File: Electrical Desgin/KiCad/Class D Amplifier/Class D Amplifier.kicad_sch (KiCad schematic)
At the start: 1 part

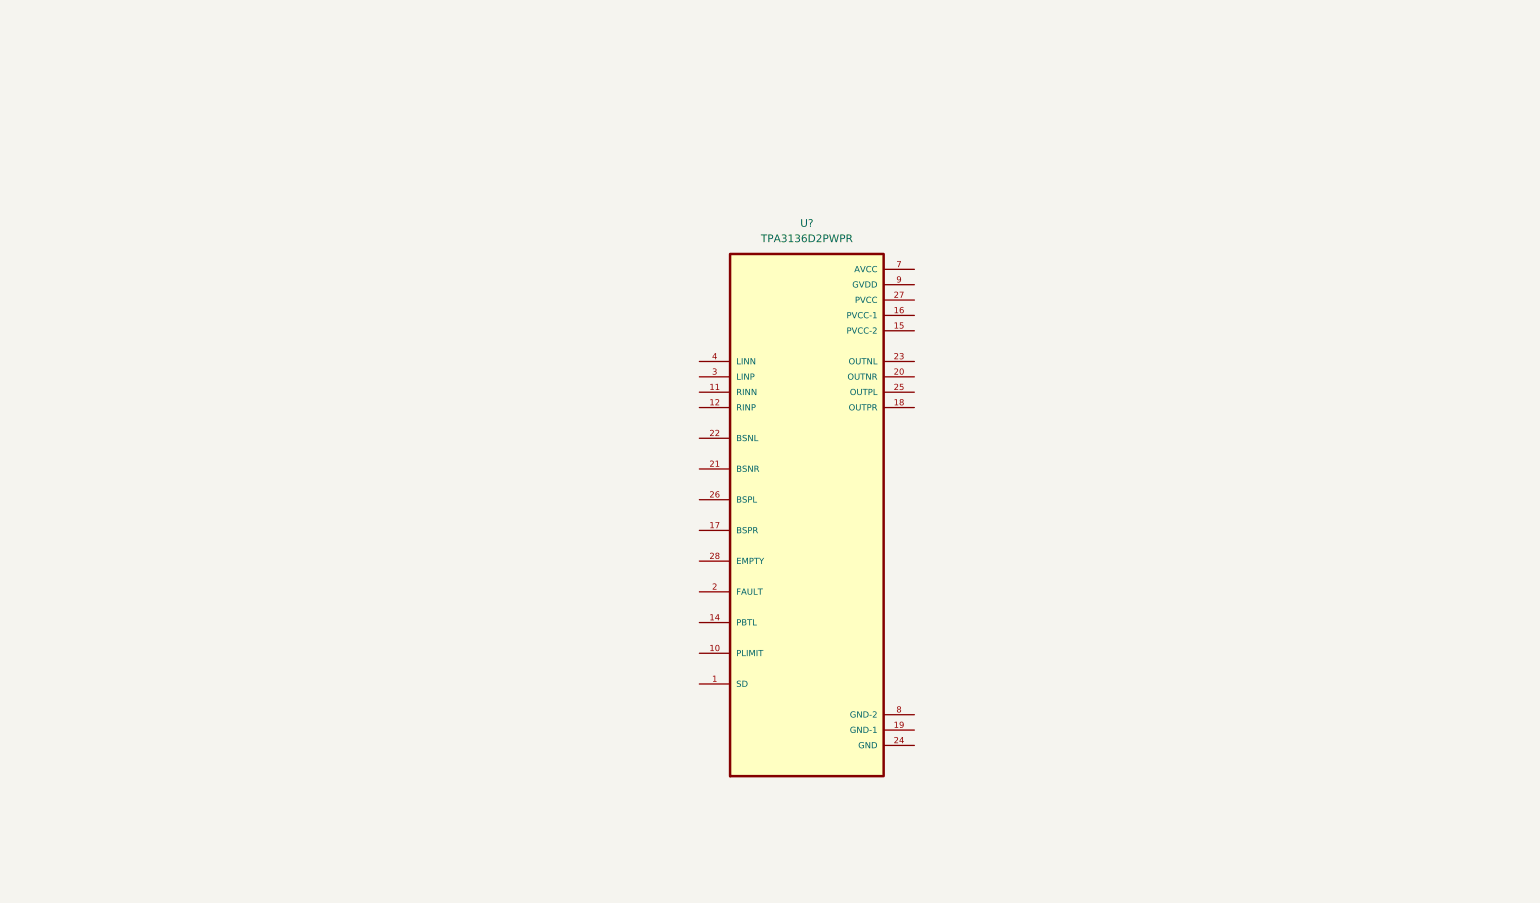
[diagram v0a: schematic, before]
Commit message: generate amplifier schematic
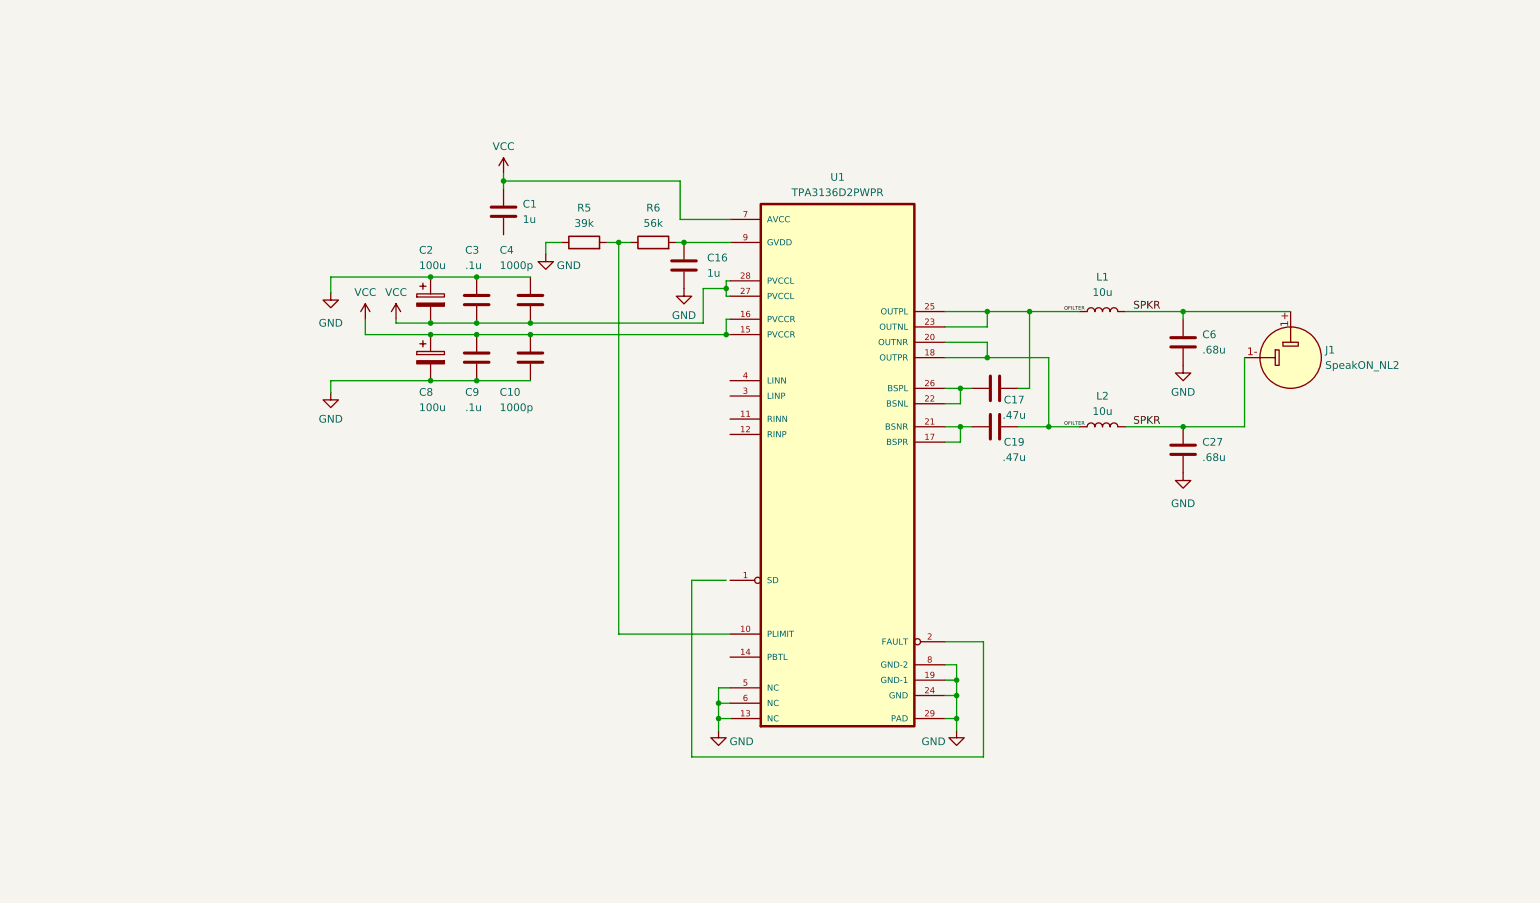
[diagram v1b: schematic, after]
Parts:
- removed U?: TPA3136D2PWPR, TPA3136D2PWPR:IC_TPS61196PWPRQ1, symbol TPA3136D2PWPR:TPA3136D2PWPR
- added C1, C16: 1u, symbol Device:C
- added C10, C4: 1000p, symbol Device:C
- added C17, C19: .47u, symbol Device:C
- added C2, C8: 100u, symbol Device:C_Polarized
- added C27, C6: .68u, symbol Device:C
- added C3, C9: .1u, symbol Device:C
- added J1: SpeakON_NL2, symbol Connector_Audio:SpeakON_NL2
- added L1, L2: 10u, symbol Device:L
- added R5: 39k, symbol Device:R
- added R6: 56k, symbol Device:R
- added U1: TPA3136D2PWPR, TPA3136D2PWPR:IC_TPS61196PWPRQ1, symbol TPA3136D2PWPR:TPA3136D2PWPR
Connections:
- new net: R5.2, R6.1, U1.10 (PLIMIT)
- new net: C19.1, U1.17 (BSPR), U1.21 (BSNR)
- new net: C17.1, U1.22 (BSNL), U1.26 (BSPL)
- new net: C16.2, R6.2, U1.9 (GVDD)
- new net GND: C10.2, C16.1, C2.1, C27.2, C3.1, C4.1, C6.2, C8.2, C9.2, R5.1, U1.13 (NC), U1.19 (GND-1), U1.24 (GND), U1.29 (PAD), U1.5 (NC), U1.6 (NC), U1.8 (GND-2)
- new net OFILTER: C17.2, C19.2, L1.1, L2.1, U1.18 (OUTPR), U1.20 (OUTNR), U1.23 (OUTNL), U1.25 (OUTPL)
- new net SPKR: C27.1, C6.1, J1.1+, J1.1-, L1.2, L2.2
- new net VCC: C1.1, C10.1, C2.2, C3.2, C4.2, C8.1, C9.1, U1.15 (PVCCR), U1.16 (PVCCR), U1.27 (PVCCL), U1.28 (PVCCL), U1.7 (AVCC)

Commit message: class D schematic update
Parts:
- added C10: .27u, symbol Device:C
- added C8: 0.27u, symbol Device:C
- added J1: AudioJack3, symbol Connector_Audio:AudioJack3
- added R1, R2: 100k, symbol Device:R
- added R5, R6: 1k, symbol Device:R
- C13: renamed from C6; value .68u -> 1u
- C14: renamed from C27; value .68u -> 1u
- J2: renamed from J1; value SpeakON_NL2 -> SpeakON_NL2MDXX-V
- L1, L2: value 10u -> 33u
- renumbered C2 to C1, C17 to C11, C19 to C12, C8 to C2, C9 to C4, C1 to C5, C4 to C6, C10 to C7, C16 to C9, R5 to R3, R6 to R4
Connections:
- net GND: now also C5.2, C10.2, J1.S
- net OFILTER: now also C11.1, C12.1, U1.17 (BSPR), U1.21 (BSNR), U1.22 (BSNL), U1.26 (BSPL)
- net VCC: now also R1.1, R2.1
- net /SHUTDOWN: now reaches U1.1 (SD)
- net /SHUTDOWN: now also U1.2 (FAULT), R1.2
- net RINN: now reaches U1.11 (RINN)
- net RINN: now also C10.1
- net RINP: now reaches U1.12 (RINP)
- net RINP: now also C8.1
- net at U1.14 (PBTL): now also R2.2
- new net: J1.T, R6.1
- new net: J1.R, R5.2
- new net AMPIN: C8.2, R5.1, R6.2
- no-connect marks 0 -> 2
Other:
- note added: "Mono Summing Input"
- note added: "Output Filtering"
- note added: "Output to 8ohm speaker"
- note added: "Power Supply Filtering & Decoupling"
- note added: "Selected for f_{c} = 20 Hz"
- note added: "Selected values for driving 8ohm load"
- note added: "TI 20W Class-D Audio Amplifier"
- company: (none) -> Portland State University
- title: (none) -> 20W Mono Class-D Audio Amplifier
- moved on the sheet: C1, C11, C12, C13, C14, C2, C3, C4, C5, C6, C7, C9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
